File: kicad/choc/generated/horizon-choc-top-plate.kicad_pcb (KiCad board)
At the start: 2 copper layers, 36 x 34 mm, 5 parts

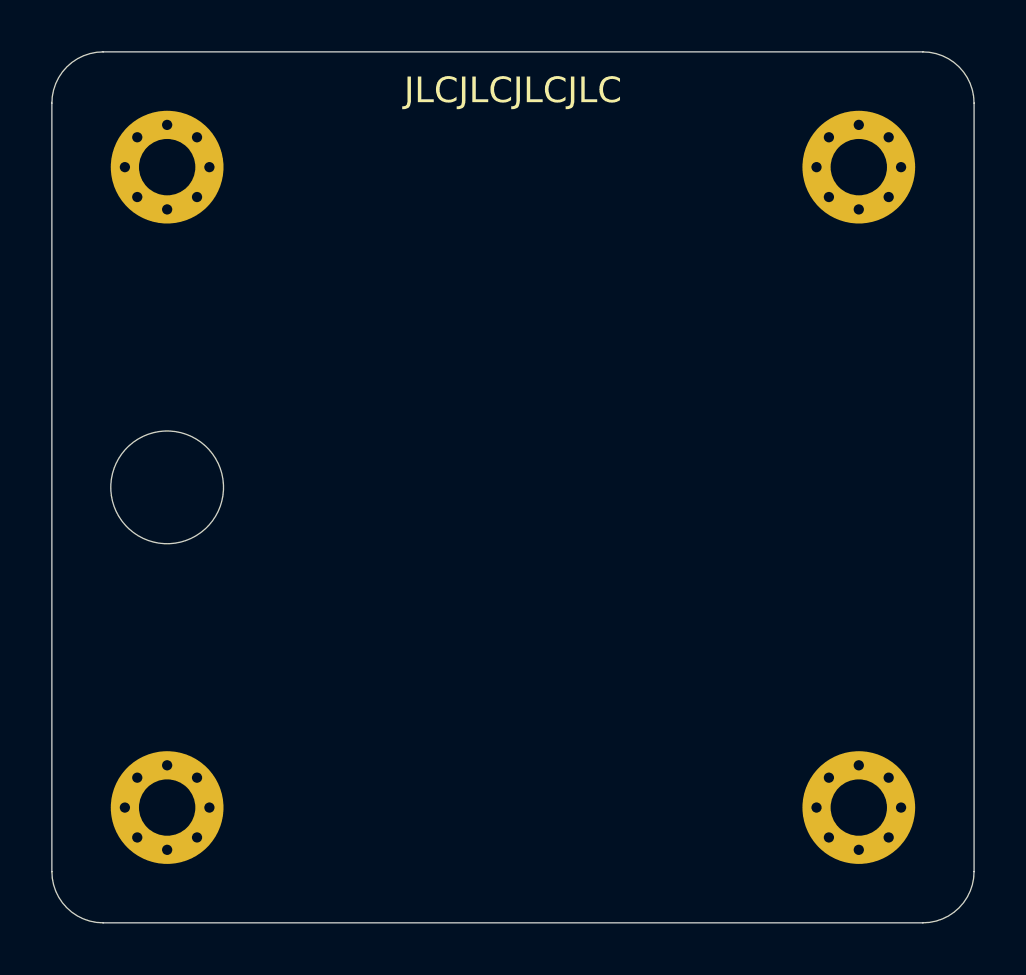
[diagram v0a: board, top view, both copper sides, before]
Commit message: Preserve logos on plate PCBs
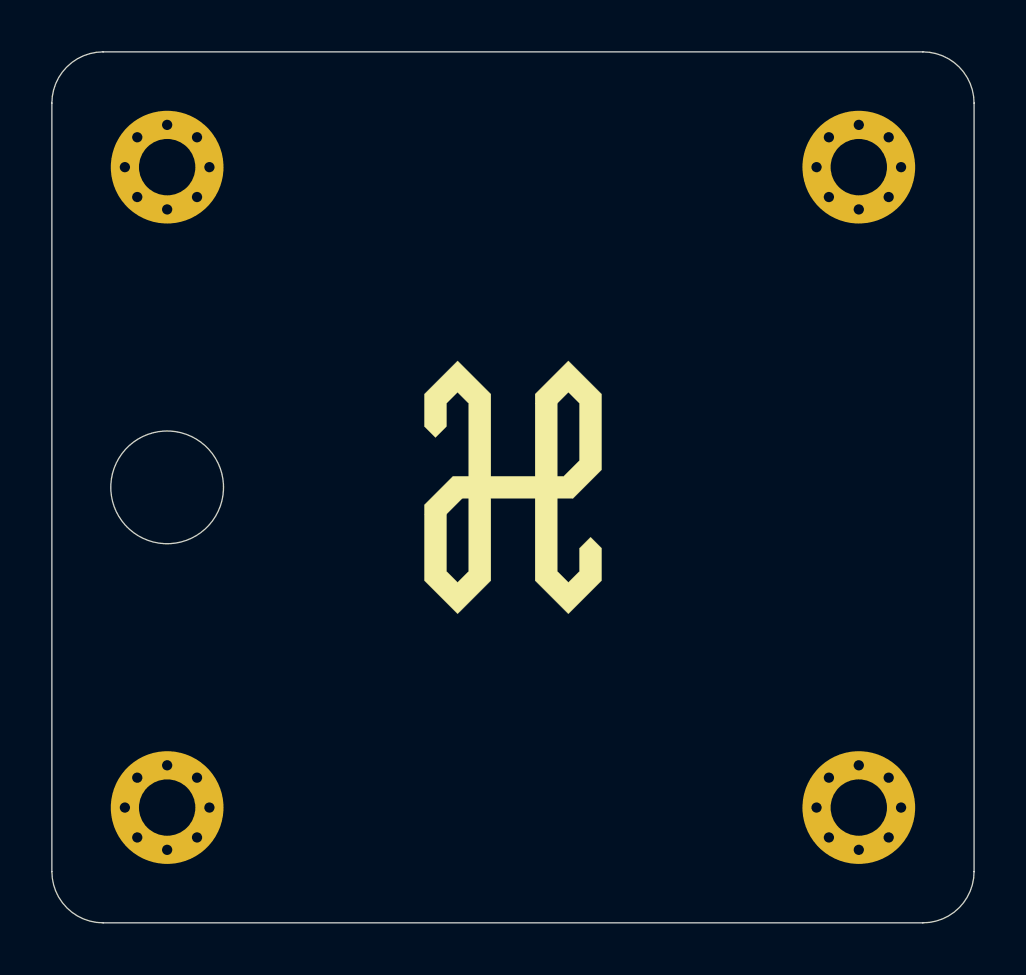
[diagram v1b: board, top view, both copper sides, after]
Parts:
- added ?: Logo-Top, horizon-footprints:Logo_Horizon_H, F.Cu at (202.0, 112.0)
- added ?: Logo-Bottom, horizon-footprints:Logo_Horizon_Small, B.Cu at (202.0, 100.5)
- added ?: PRO-MICRO, horizon-footprints:Pro-Micro, F.Cu at (202.0, 95.0)
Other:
- board text added: "github.com/skarrmann/horizon"
- board text added: "rev2 | Choc"

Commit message: Remove unused footprints and other files. Update readme. Prepare for production!
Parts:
- moved ? 11.0 mm to (202.0, 111.5)
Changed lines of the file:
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@@
   )
   (module horizon-footprints:Logo_Horizon_Small (layer B.Cu)
-    (at 202 100.5 180)
+    (at 202 111.5 180)
     (fp_text reference "" (at 0 -2) (layer B.SilkS) hide
       (effects (font (size 1.524 1.524) (thickness 0.3)) (justify mirror))
@@
   (gr_arc (start 186 127) (end 184 127) (angle -90) (layer Edge.Cuts) (width 0.05))
   (gr_arc (start 186 97) (end 186 95) (angle -90) (layer Edge.Cuts) (width 0.05))
-  (gr_text "rev2 | Choc" (at 202 104.5) (layer B.SilkS)
+  (gr_text "rev2 | Choc" (at 202 115.5) (layer B.SilkS)
     (effects (font (size 1 1) (thickness 0.15)) (justify mirror))
   )
-  (gr_text JLCJLCJLCJLC (at 202 106.5) (layer B.SilkS)
+  (gr_text JLCJLCJLCJLC (at 202 127.5) (layer B.SilkS)
     (effects (font (size 1 1) (thickness 0.15)) (justify mirror))
   )
